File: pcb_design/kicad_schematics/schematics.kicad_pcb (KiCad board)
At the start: 2 copper layers, 29 parts, among them J10 LED-HSF08A/B, J11 BUTTON-HS-KEY1B, J6 PICKIT, J7 I2C_Communication_Protocol, J8 M22-2510205, J9 SG90, U1 PIC24FJ64GA702-I_SO, U2 ESP8266-01_ESP-01, U3 LM1117LD-3.3, Y2 16MHz crystal

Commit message: Prva verzija pcb.
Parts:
- moved U2 54.3 mm to (179.1, 50.9)
- moved J9 51.5 mm to (161.8, 53.0)
- moved U3 41.5 mm to (136.8, 52.0)
- moved R1 39.5 mm to (115.6, 77.8), turned to 180 degrees
- moved J6 37.2 mm to (114.8, 60.2), turned to -90 degrees
- moved J8 35.0 mm to (119.8, 51.2), turned to -90 degrees
- moved C10 32.5 mm to (126.8, 52.2), turned to 90 degrees
- moved R2 31.6 mm to (124.5, 73.0)
- moved C16 29.7 mm to (132.8, 61.5)
- moved J11 29.2 mm to (126.2, 63.2), turned to 90 degrees
- moved C2 27.4 mm to (153.5, 59.0), turned to 90 degrees
- moved Y2 27.4 mm to (132.4, 65.4), turned to 90 degrees
- moved C12 27.0 mm to (170.0, 68.3), turned to 90 degrees
- moved C13 26.9 mm to (170.0, 72.0), turned to -90 degrees
- moved J7 26.8 mm to (159.2, 76.5), turned to 90 degrees
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
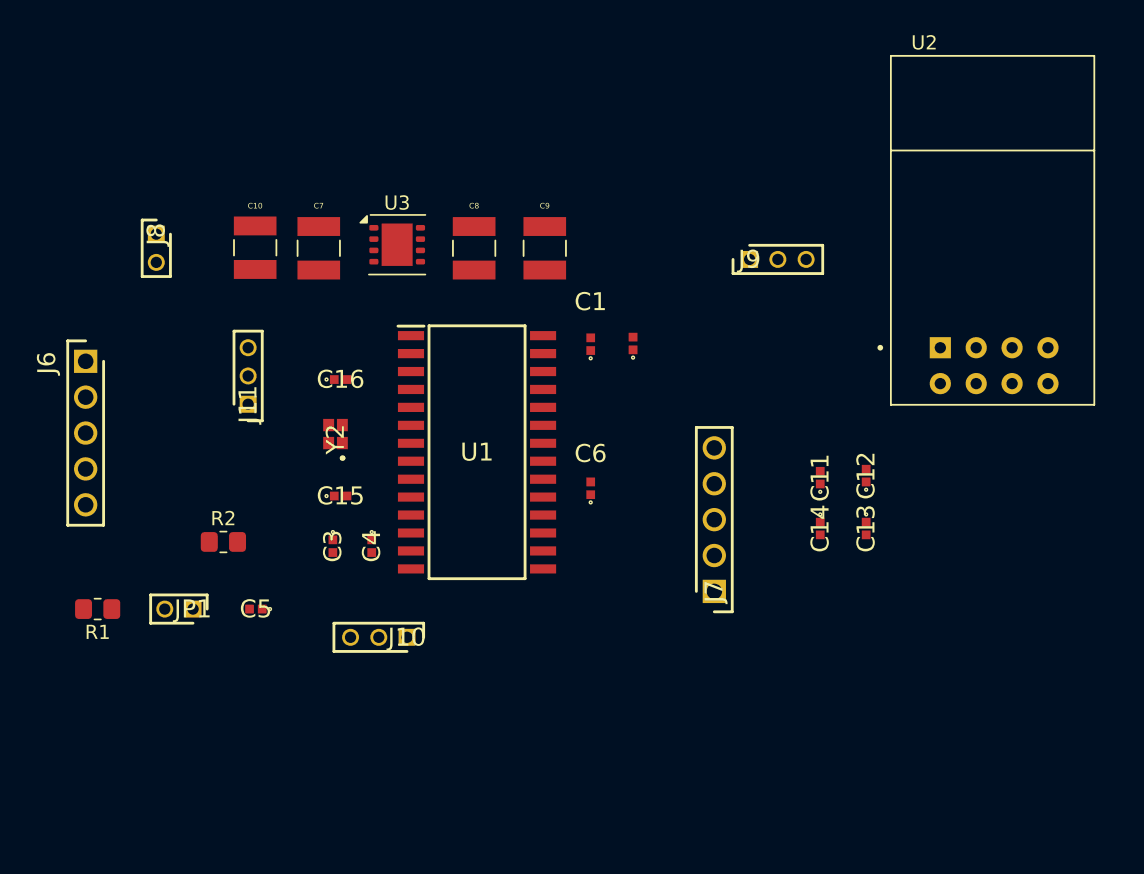
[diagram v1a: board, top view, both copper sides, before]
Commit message: Inicijalno rutiranje, dodani i neki 3d modeli
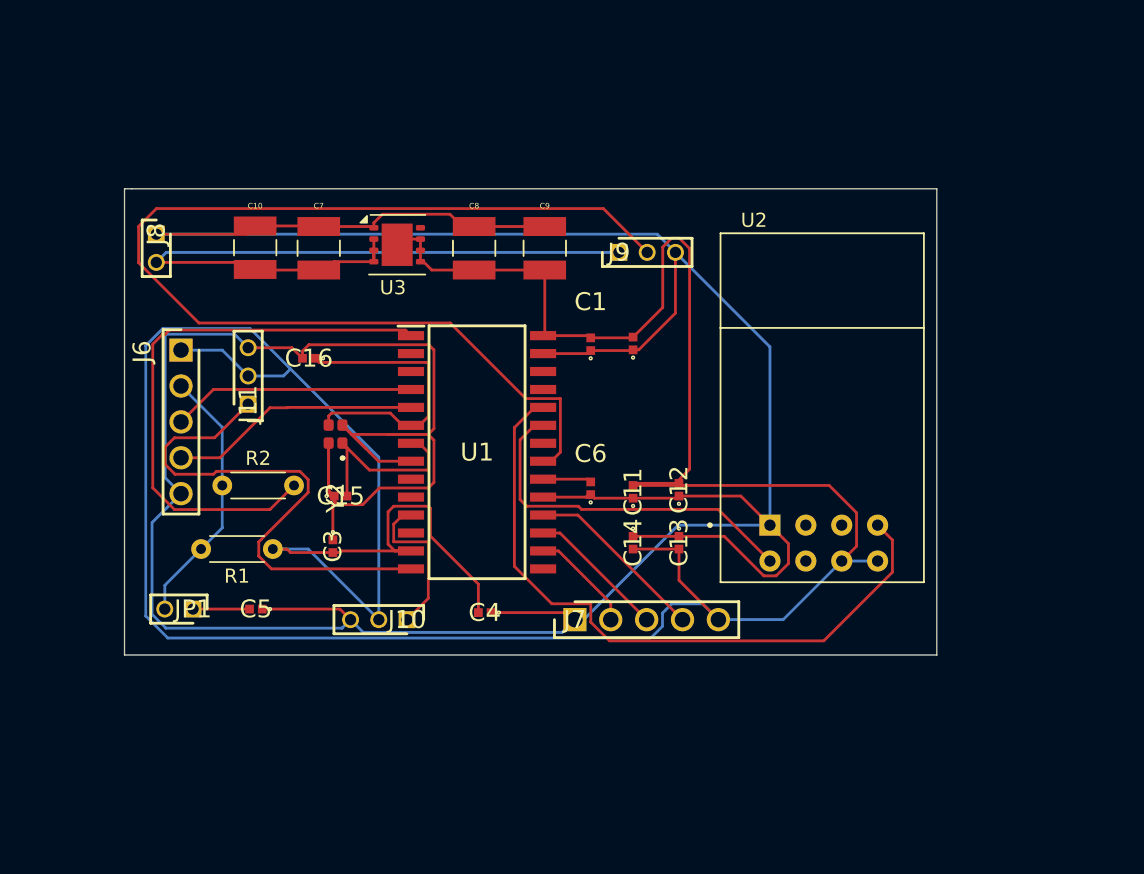
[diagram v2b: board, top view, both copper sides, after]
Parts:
- R1, R2: footprint Resistor_SMD:R_0805_2012Metric_Pad1.20x1.40mm_HandSolder -> Resistor_THT:R_Axial_DIN0204_L3.6mm_D1.6mm_P5.08mm_Horizontal
- moved U2 17.4 mm to (167.0, 63.5)
- moved C11 13.3 mm to (153.5, 69.5)
- moved C12 13.3 mm to (156.8, 69.3)
- moved C13 13.3 mm to (156.8, 73.0)
- moved C14 13.3 mm to (153.5, 73.0)
- moved R1 13.1 mm to (128.0, 73.5)
- moved J7 10.1 mm to (149.4, 78.5), turned to 0 degrees
- moved C4 9.28 mm to (143.0, 78.0), turned to 180 degrees
- moved J9 9.26 mm to (152.5, 52.5)
- moved J6 6.80 mm to (121.5, 59.4)
- moved R2 4.00 mm to (124.4, 69.0)
- moved C16 2.70 mm to (130.6, 60.0), turned to 180 degrees
- moved J10 1.25 mm to (137.5, 78.5)
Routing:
- net GND: track 0.00 -> 283.7 mm
- net +3.3V: track 0.00 -> 235.5 mm
- net /PWM: track 0.00 -> 79.5 mm
- net +Vin: track 0.00 -> 51.3 mm
- net /RB13: track 0.00 -> 47.9 mm
- net Net-(U1-~{MCLR}): track 0.00 -> 40.4 mm
- net /RB5: track 0.00 -> 37.1 mm
- net /RB11: track 0.00 -> 25.8 mm
- net /RB2: track 0.00 -> 20.3 mm
- net /MCLR: track 0.00 -> 18.7 mm
- net /PGC: track 0.00 -> 17.8 mm
- net /PGD: track 0.00 -> 17.2 mm
- net /RB3: track 0.00 -> 13.5 mm
- net /I2C_SDA_1: track 0.00 -> 12.9 mm
- net /RB4: track 0.00 -> 11.3 mm
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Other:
- board outline added: 57.5 x 33 mm

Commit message: Dodani modeli ostalih komponenata u models, Podebljane zice koje nose napajanje, wifi modul okrenut, dodane oznake elemenata
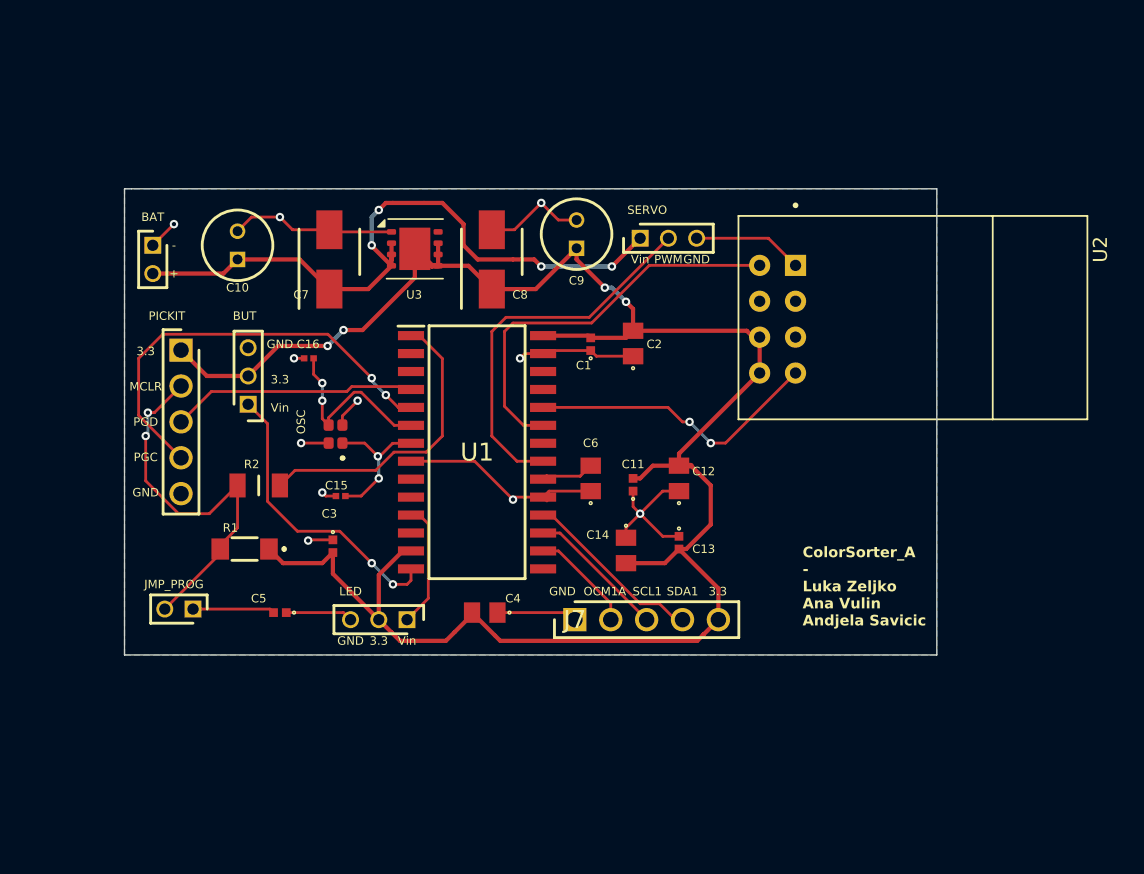
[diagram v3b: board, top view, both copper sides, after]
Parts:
- C10, C9: footprint C_Polarized_Tantalum-10u:CAPPC3528X210N -> C_Electrolytic_10uF:CAPPRD200W50D500H1250
- C12, C14, C2, C4, C6: footprint C_Ceramic_100n:C0402 -> C_Ceramic_10u:C0805
- C15, C16: footprint C_Ceramic_100n:C0402 -> C_Ceramic-10pF:CAPC0603X33N
- C7, C8: footprint C_Polarized_Tantalum-10u:CAPPC3528X210N -> C_Electrolytic_0.1uF:CAPAE430X550N
- R1: footprint Resistor_THT:R_Axial_DIN0204_L3.6mm_D1.6mm_P5.08mm_Horizontal -> R_SMD_10kOhm:ERA8KEB1004V
- R2: footprint Resistor_THT:R_Axial_DIN0204_L3.6mm_D1.6mm_P5.08mm_Horizontal -> R_SMD_200Ohm:RESC3216X70N
- moved U2 8.90 mm to (173.3, 57.2), turned to -90 degrees
- moved R2 2.58 mm to (127.0, 69.0)
- moved C9 2.25 mm to (149.5, 52.2)
- moved R1 2.00 mm to (126.0, 73.5)
- moved J9 1.80 mm to (154.0, 51.5)
- moved C5 1.72 mm to (128.5, 78.0)
- moved C10 1.50 mm to (125.5, 53.0)
- moved C8 1.48 mm to (143.5, 53.0)
- moved U3 1.28 mm to (138.1, 52.2)
- moved C7 1.09 mm to (132.0, 53.0)
- moved J8 0.83 mm to (119.5, 52.0)
- moved C12 0.80 mm to (156.8, 68.5)
- moved C14 0.74 mm to (153.0, 73.6)
- moved C6 0.70 mm to (150.5, 68.5)
- moved C11 0.50 mm to (153.5, 69.0)
- renumbered J10 to LED
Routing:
- net GND: track 283.7 -> 81.6 mm, vias 0 -> 11
- net +3.3V: track 235.5 -> 139.9 mm, vias 0 -> 4
- net /PWM: track 79.5 -> 27.0 mm
- net /RB13: track 47.9 -> 21.0 mm, vias 0 -> 2
- net Net-(U1-~{MCLR}): track 40.4 -> 21.3 mm
- net /RB5: track 37.1 -> 21.0 mm, vias 0 -> 2
- net /PGC: track 17.8 -> 30.5 mm, vias 0 -> 2
- net /MCLR: track 18.7 -> 27.2 mm, vias 0 -> 2
- net /RB2: track 20.3 -> 13.8 mm, vias 0 -> 2
- net /RB3: track 13.5 -> 10.7 mm, vias 0 -> 2
- net /RB11: track 25.8 -> 28.6 mm
- net /RB4: track 11.3 -> 8.89 mm
- net +Vin: track 51.3 -> 49.0 mm, vias 0 -> 4
- net Net-(JP1-A): track 4.00 -> 5.80 mm
- net Net-(U1-VCAP): track 3.45 -> 4.13 mm
- added copper zone on B.Cu, net GND
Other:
- board text added: "+"
- board text added: "-"
- board text added: "3.3"
- board text added: "BAT"
- board text added: "BUT"
- board text added: "C1"
- board text added: "C10"
- board text added: "C11"
- board text added: "C12"
- board text added: "C13"
- board text added: "C14"
- board text added: "C15"
- board text added: "C16"
- board text added: "C2"
- board text added: "C3"
- board text added: "C4"
- board text added: "C5"
- board text added: "C6"
- board text added: "C7"
- board text added: "C8"
- board text added: "C9"
- board text added: "ColorSorter_A - Luka Zeljko Ana Vulin Andjela Savicic"
- board text added: "GND"
- board text added: "JMP_PROG"
- board text added: "MCLR"
- board text added: "OCM1A"
- board text added: "OSC"
- board text added: "PGC"
- board text added: "PGD"
- board text added: "PICKIT"
- board text added: "PWM"
- board text added: "R1"
- board text added: "R2"
- board text added: "SCL1"
- board text added: "SDA1"
- board text added: "SERVO"
- board text added: "U3"
- board text added: "Vin"

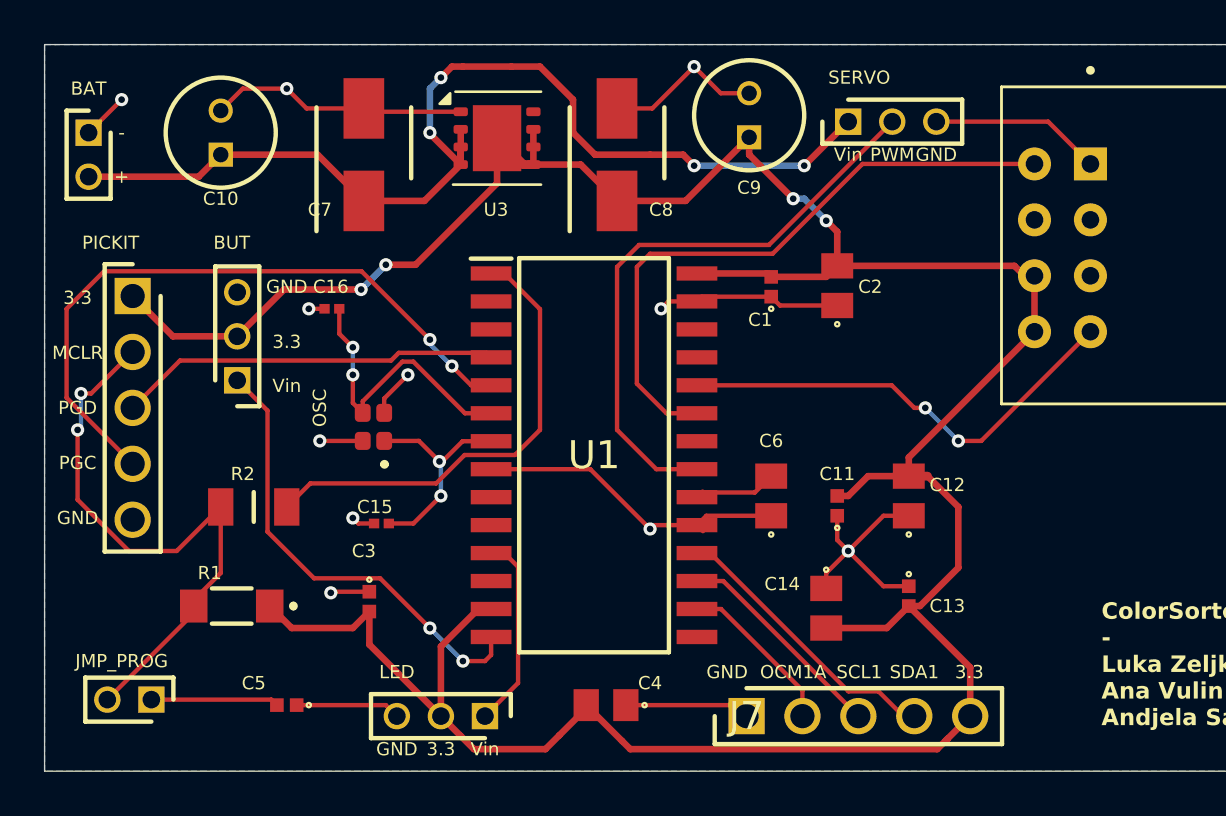
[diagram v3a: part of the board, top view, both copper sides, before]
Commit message: Ispravljene greske sa sastanka
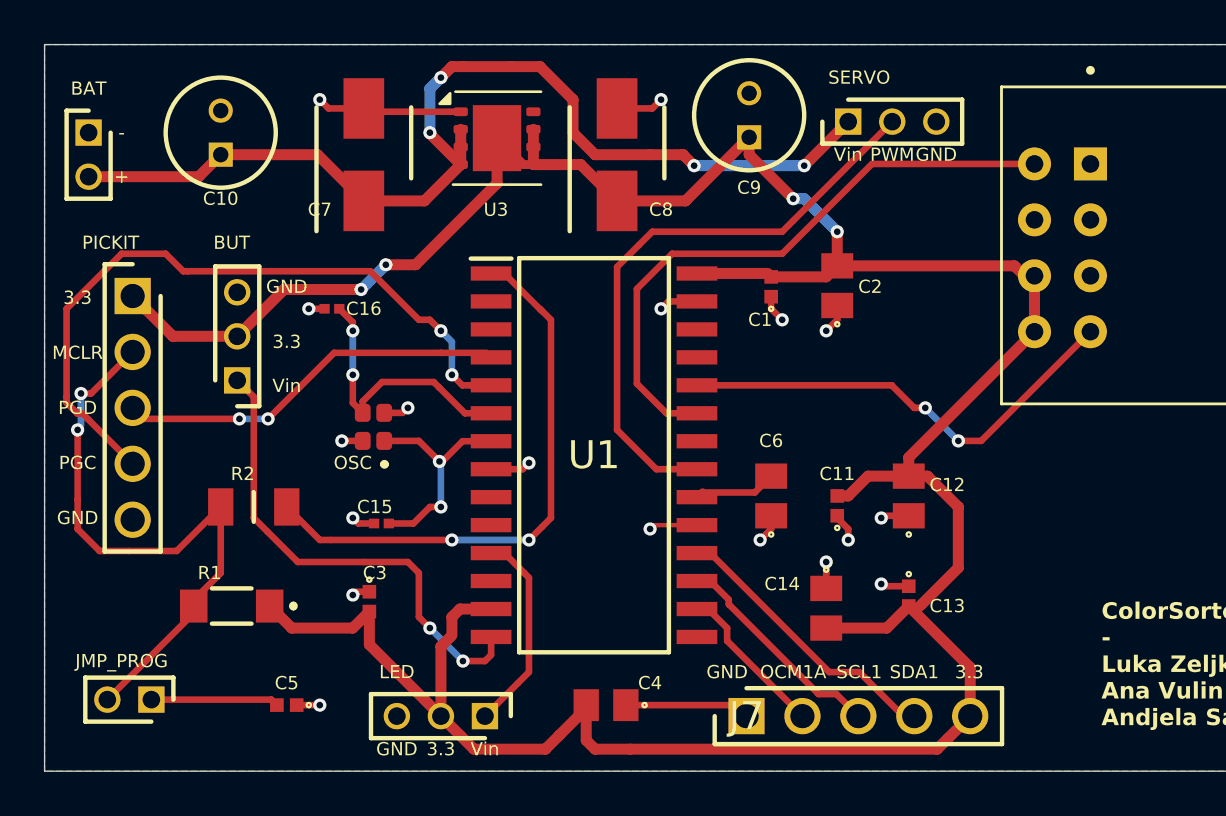
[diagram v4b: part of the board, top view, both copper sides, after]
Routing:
- net GND: track 81.6 -> 36.2 mm, vias 11 -> 18
- net Net-(U1-~{MCLR}): track 21.3 -> 25.8 mm, vias 0 -> 2
- net /PGC: track 30.5 -> 33.0 mm
- net +3.3V: track 139.9 -> 141.3 mm
- net /RB5: track 21.0 -> 22.1 mm
- net /MCLR: track 27.2 -> 28.0 mm
- net /RB2: track 13.8 -> 13.1 mm
- net /RB11: track 28.6 -> 28.0 mm
- net /PGD: track 17.4 -> 17.8 mm, vias 0 -> 2
